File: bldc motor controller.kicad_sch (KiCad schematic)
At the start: 48 parts, among them J1 Conn_01x04_Pin, U1 C47023655, U3 C529358, U6 C126671

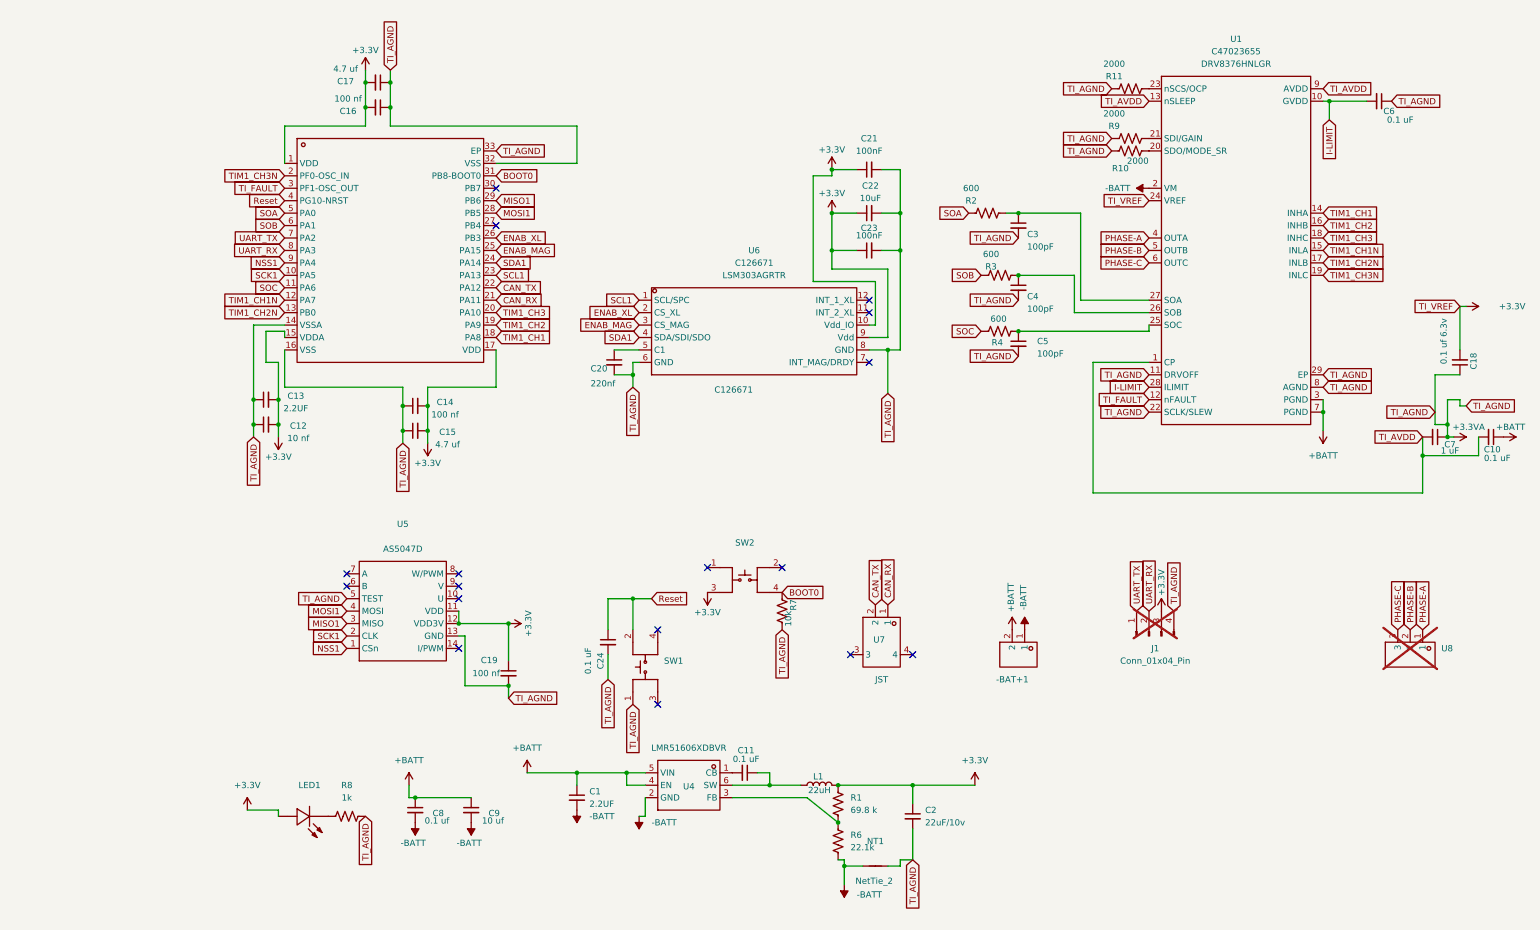
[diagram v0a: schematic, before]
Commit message: Updated schematic with new imu
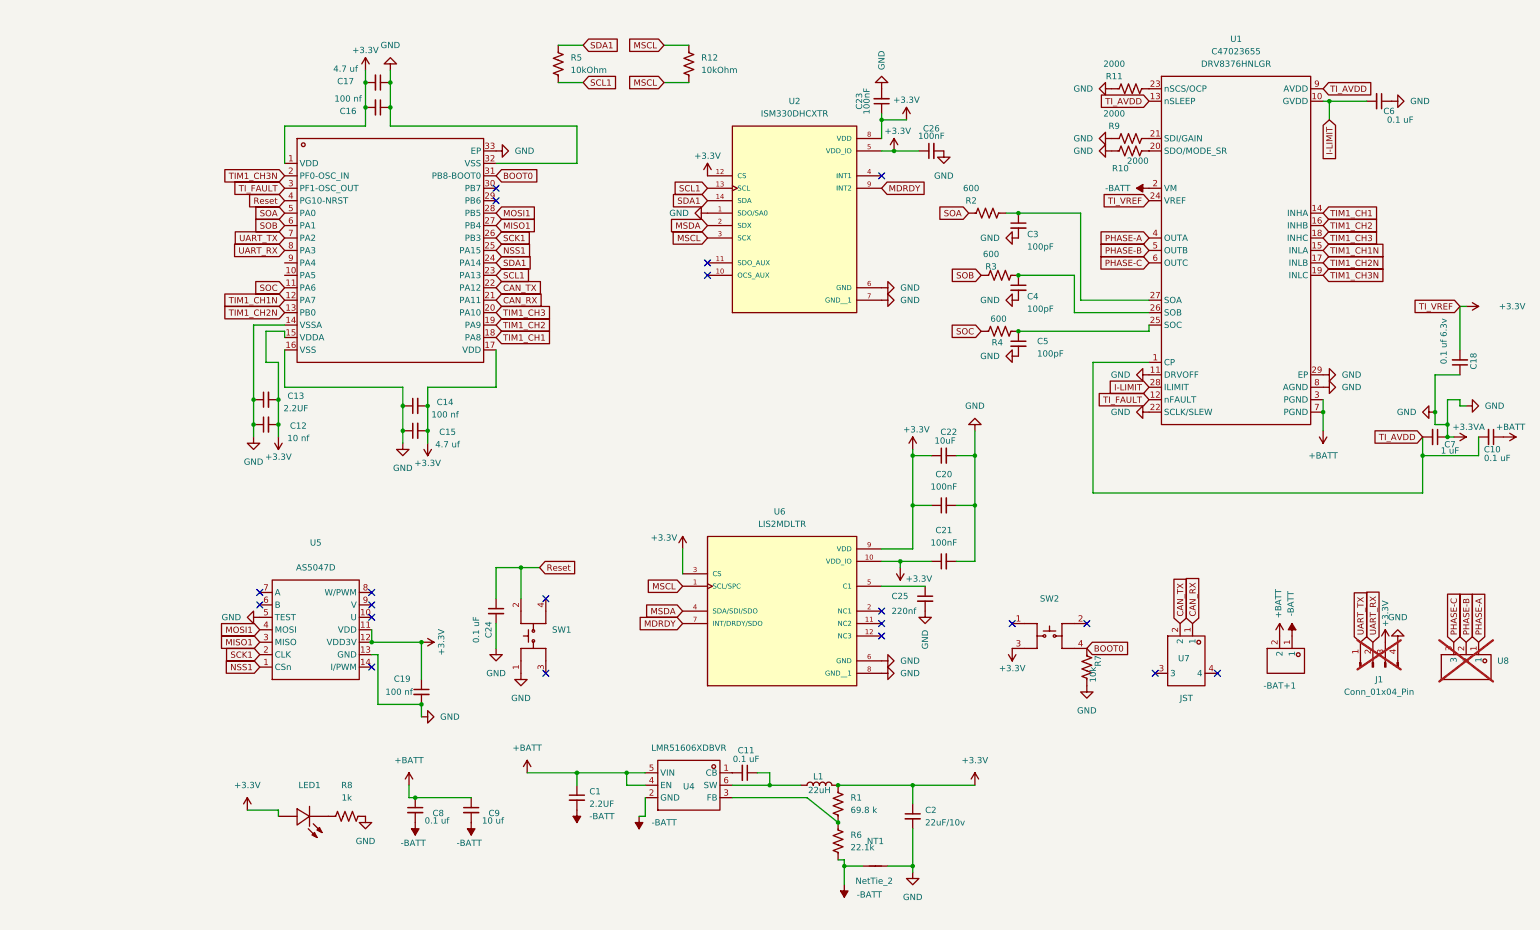
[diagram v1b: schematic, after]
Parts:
- removed U6: C126671, bldc-motor-footprints:LGA-12_L2.0-W2.0-P0.50-BL, symbol bldc controller:LSM303AGRTR
- added C25: 220nf, Capacitor_SMD:C_01005_0402Metric, symbol Device:C_Small
- added C26: 100nF, Capacitor_SMD:C_01005_0402Metric, symbol Device:C_Small
- added R12, R5: 10kOhm, Resistor_SMD:R_0402_1005Metric, symbol Device:R_US
- added U2: ISM330DHCXTR, bldc-motor-footprints:PQFN50P250X300X86-14N, symbol bldc controller:ISM330DHCXTR
- added U6: LIS2MDLTR, bldc-motor-footprints:PQFN50P200X200X70-12N, symbol bldc controller:LIS2MDLTR
- C20: value 220nf -> 100nF
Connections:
- net ENAB_MAG is gone; now on net NSS1: U3.25 (PA15)
- net ENAB_XL is gone; now on net SCK1: U3.26 (PB3)
- net +3.3V: now also C20.1, C26.1, U2.12 (CS), U2.5 (VDD_IO), U2.8 (VDD), U6.10 (VDD_IO), U6.3 (CS), U6.9 (VDD)
- net +3.3VA: now also C25.2, C26.2, U2.1 (SDO/SA0), U2.6 (GND), U2.7 (GND__1), U6.6 (GND), U6.8 (GND__1)
- net MISO1: now also U3.27 (PB4); no longer U3.29 (PB6)
- net NSS1: no longer U3.9 (PA4)
- net SCK1: no longer U3.10 (PA5)
- net SCL1: now also R5.2, U2.13 (SCL)
- net SDA1: now also R5.1, U2.14 (SDA)
- new net: C25.1, U6.5 (C1)
- new net MDRDY: U2.9 (INT2), U6.7 (INT/DRDY/SDO)
- new net MSCL: R12.1, R12.2, U2.3 (SCX), U6.1 (SCL/SPC)
- new net MSDA: U2.2 (SDX), U6.4 (SDA/SDI/SDO)
- no-connect marks 17 -> 20
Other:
- moved on the sheet: -BAT+1, C19, C21, C22, C23, C24, J1, R7, SW1, SW2, U5, U7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

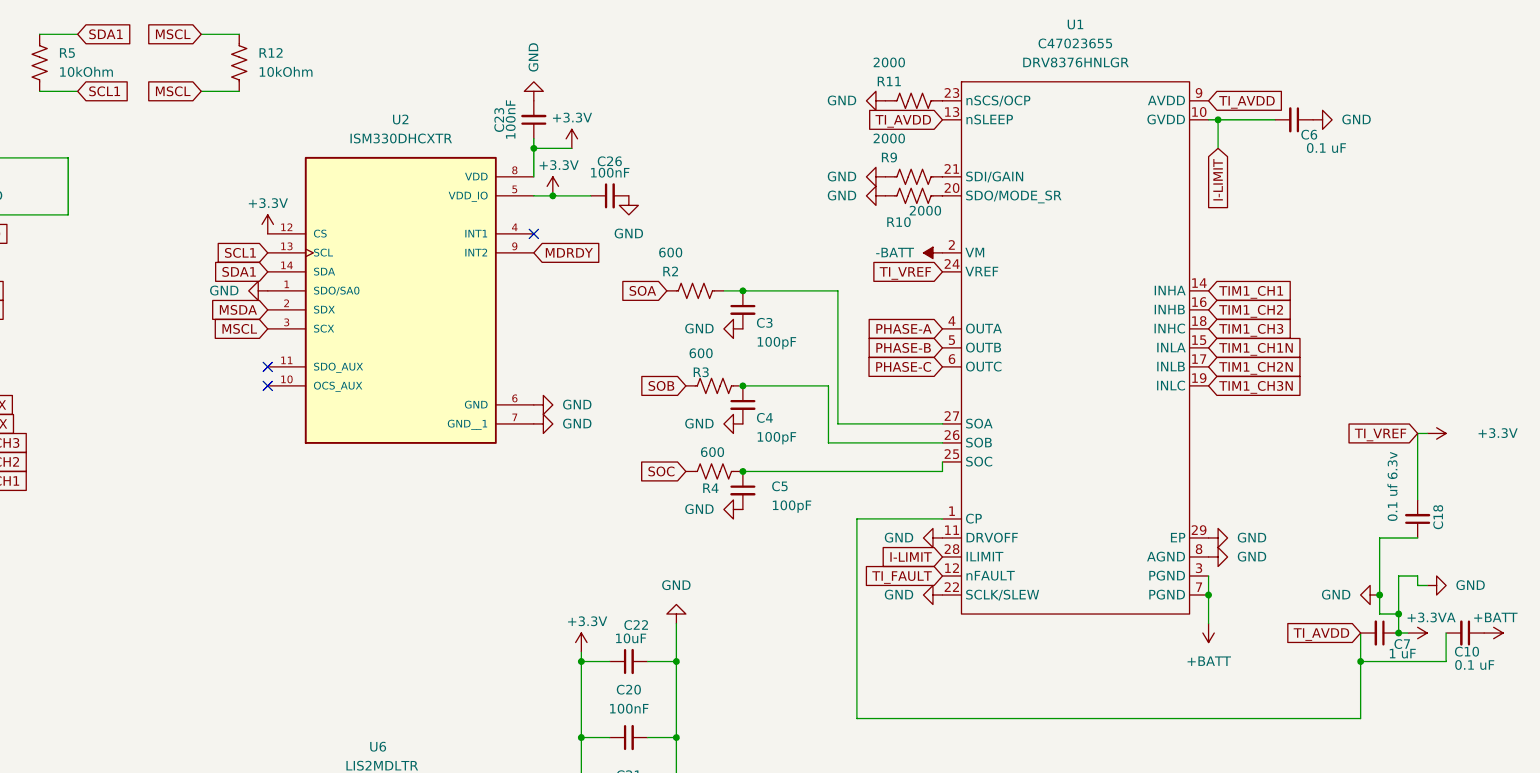
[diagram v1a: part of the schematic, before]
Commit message: Updated PCB, need to do some tweaks on motor controller schematic side
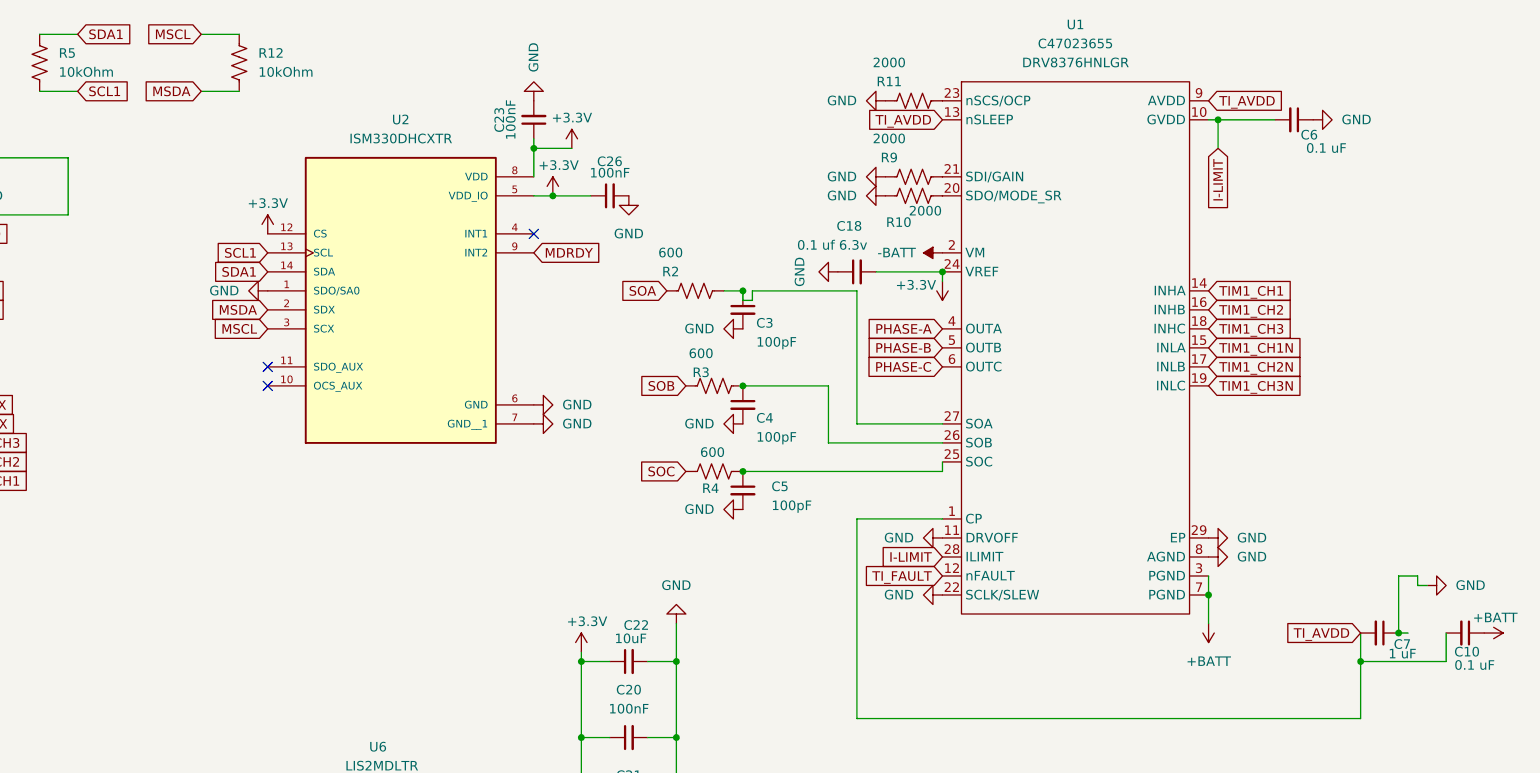
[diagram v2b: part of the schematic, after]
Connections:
- net MSCL: no longer R12.2
- net MSDA: now also R12.2
- net +3.3VA renamed GND
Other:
- moved on the sheet: C18

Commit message: Final push of the day
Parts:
- J1: now fitted; now left out of the parts list
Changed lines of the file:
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@@
 		(unit 1)
 		(exclude_from_sim no)
-		(in_bom yes)
+		(in_bom no)
 		(on_board yes)
-		(dnp yes)
+		(dnp no)
 		(fields_autoplaced yes)
 		(property "Reference" "J1"

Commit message: Wooo added a can transciever
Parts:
- added C27: 100 nf, Capacitor_SMD:C_01005_0402Metric, symbol Device:C_Small
- added U9: ~, bldc-motor-footprints:SON-8_L3.0-W3.0-P0.65-LS2.9-BL-EP, symbol bldc controller:TCAN3413DRBR
- J1: now in the parts list
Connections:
- net +3.3V: now also C27.1, U9.3 (VCC)
- net CAN_RX: now also U9.4 (RXD); no longer U7.1
- net CAN_TX: now also U9.1 (TXD); no longer U7.2
- net GND: now also C27.2, U9.2 (GND), U9.9 (PAD)
- net STB: now reaches U3.10 (PA5)
- net STB: now also U9.8 (STB)
- net SHDN: now reaches U3.9 (PA4)
- net SHDN: now also U9.5 (SHDN,VIO)
- new net C+: U7.1, U9.7 (CANH)
- new net C-: U7.2, U9.6 (CANL)
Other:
- moved on the sheet: U7

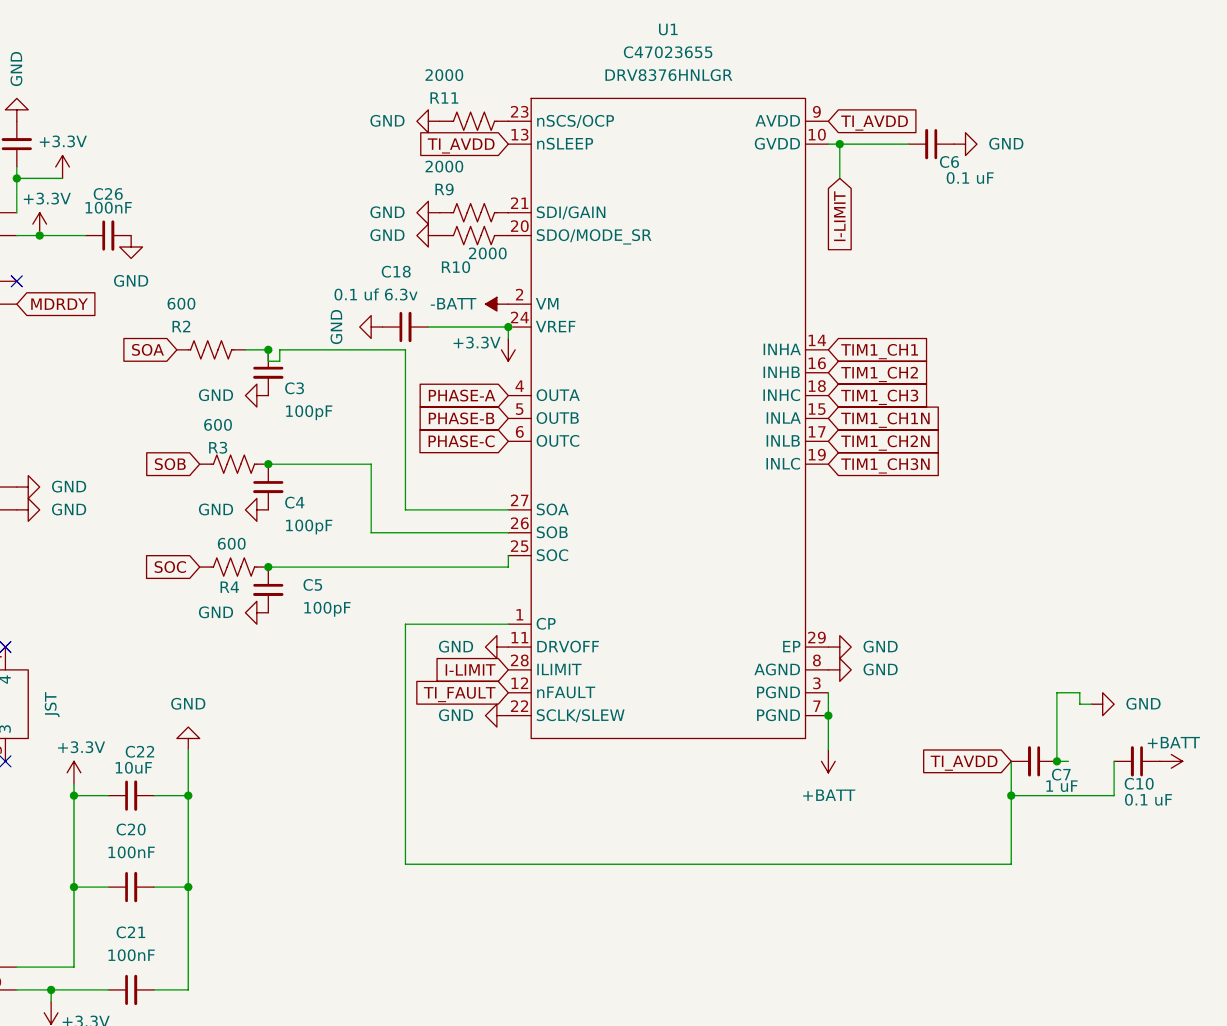
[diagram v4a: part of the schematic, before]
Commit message: Going to try to fix battery routing
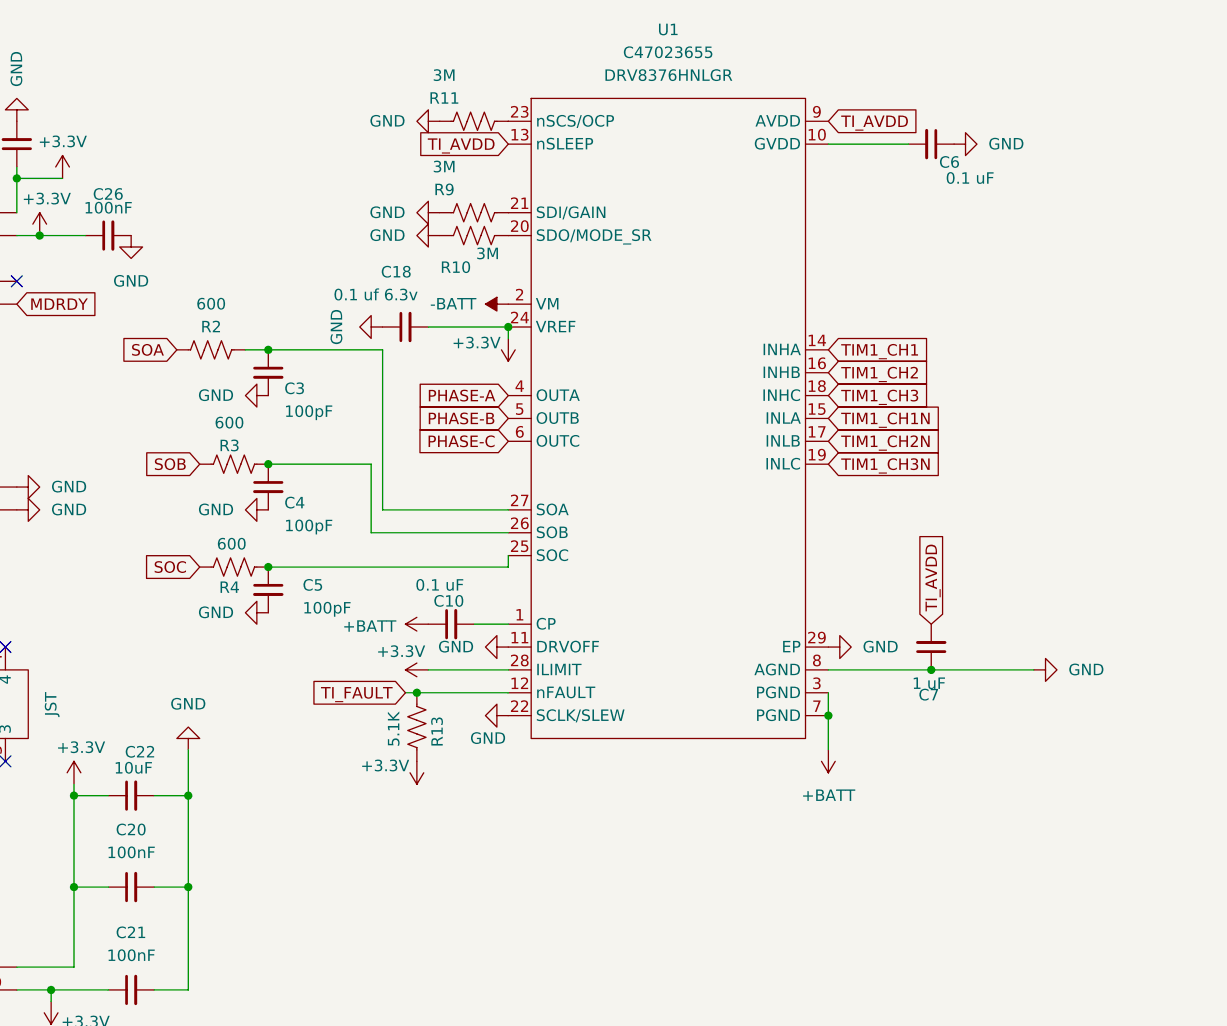
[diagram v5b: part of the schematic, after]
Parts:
- added R13: 5.1K, Resistor_SMD:R_0603_1608Metric, symbol Device:R_US
- R10, R11, R9: value 2000 -> 3M; footprint Resistor_SMD:R_01005_0402Metric -> Resistor_SMD:R_0402_1005Metric
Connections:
- net +3.3V: now also U1.28 (ILIMIT), R13.2
- net TI_AVDD: no longer C10.2, U1.1 (CP)
- net TI_FAULT: now also R13.1
- net I-LIMIT: no longer names the net of C6.2, U1.10 (GVDD)
- net I-LIMIT: no longer U1.28 (ILIMIT)
- new net: C10.2, U1.1 (CP)
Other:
- moved on the sheet: C10, C7
